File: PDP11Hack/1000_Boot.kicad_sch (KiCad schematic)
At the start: 19 parts, among them SW6 Boot Vector, U26 74HCT138, U27 74LS240

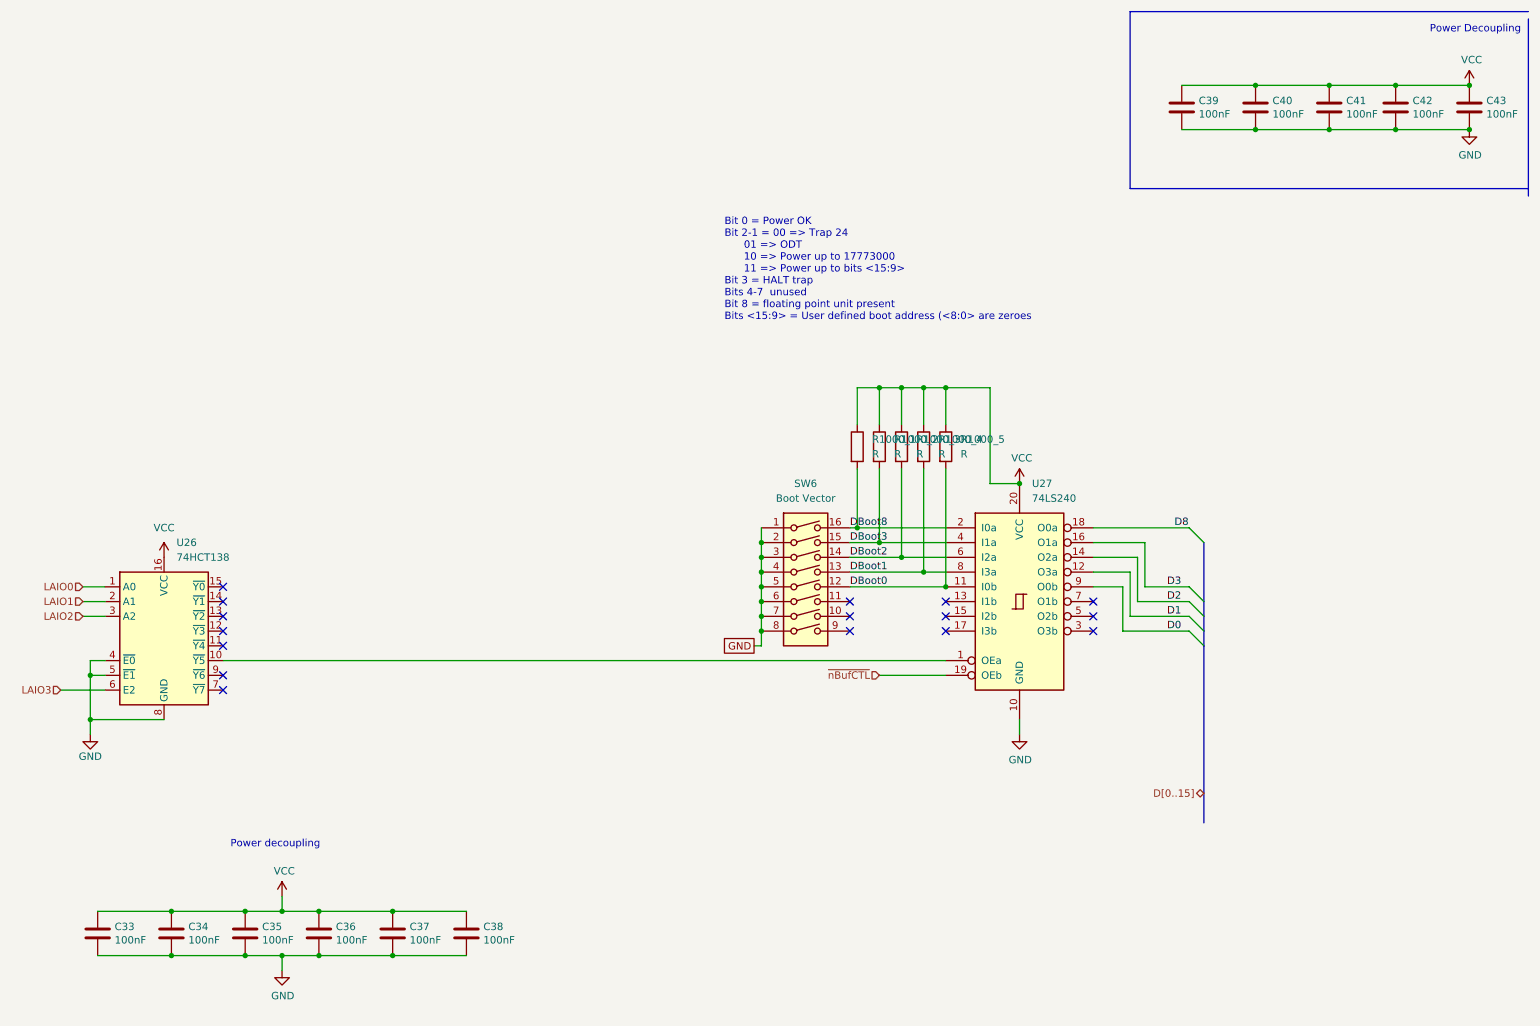
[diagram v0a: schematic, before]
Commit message: Corrections thanks to Peter Schranz on VCFED
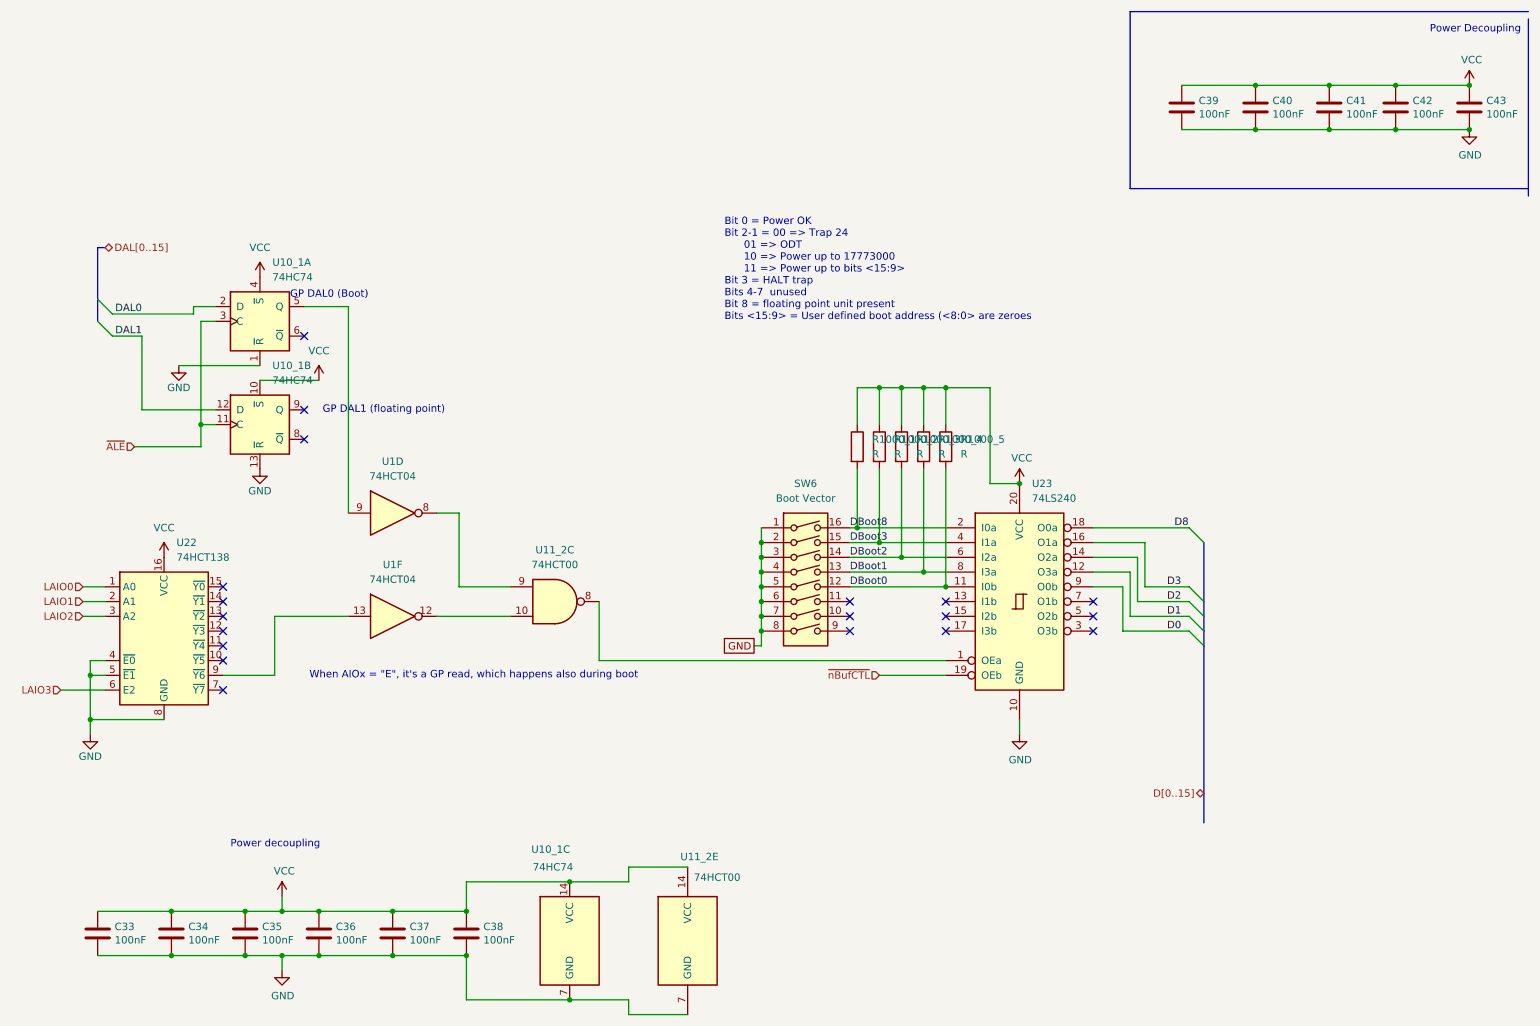
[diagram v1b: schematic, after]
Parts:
- added U1: 74HCT04, symbol 74xx:74HCT04
- added U10_1: 74HC74, symbol 74xx:74HC74
- added U11_2: 74HCT00, symbol 74xx:7400
- renumbered U26 to U22, U27 to U23
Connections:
- net GND: now also U10_1.1 (~{R}), U10_1.13 (~{R}), U10_1.7 (GND), U11_2.7 (GND)
- net VCC: now also U10_1.10 (~{S}), U10_1.14 (VCC), U10_1.4 (~{S}), U11_2.14 (VCC)
- net at U23.1 (OEa): now also U11_2.8; no longer U22.10 (~{Y5})
- net at U22.9 (~{Y6}): now also U1.13
- new net: U1.12, U11_2.10
- new net: U1.8, U11_2.9
- new net: U1.9, U10_1.5 (Q)
- new net DAL0: U10_1.2 (D)
- new net DAL1: U10_1.12 (D)
- new net ~{ALE}: U10_1.11 (C), U10_1.3 (C)
- no-connect marks 16 -> 19
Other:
- note added: "GP DAL0 (Boot)"
- note added: "GP DAL1 (floating point)"
- note added: "When AIOx = "E", it's a GP read, which happens also during boot"

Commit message: Last update, PCB creation ready
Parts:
- R1000_1, R1000_2, R1000_3, R1000_4, R1000_5: footprint (none) -> Resistor_THT:R_Axial_DIN0204_L3.6mm_D1.6mm_P7.62mm_Horizontal
- U1, U10_1, U11_2: footprint (none) -> Package_DIP:DIP-14_W7.62mm
- U22: footprint (none) -> Package_DIP:DIP-16_W7.62mm
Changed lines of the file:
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@@
 			)
 		)
-		(property "Footprint" ""
+		(property "Footprint" "Package_DIP:DIP-14_W7.62mm"
 			(at 60.96 86.36 0)
 			(effects
@@
 			)
 		)
-		(property "Footprint" ""
+		(property "Footprint" "Package_DIP:DIP-14_W7.62mm"
 			(at 111.76 116.84 0)
 			(effects
@@
 			)
 		)
-		(property "Footprint" ""
+		(property "Footprint" "Package_DIP:DIP-16_W7.62mm"
 			(at 44.45 124.46 0)
 			(effects
@@
 		(on_board yes)
 		(dnp no)
-		(fields_autoplaced yes)
 		(property "Reference" "R1000_5"
-			(at 181.61 88.9 0)
+			(at 179.07 85.09 0)
 			(effects
 				(font
@@
 			)
 		)
-		(property "Footprint" ""
+		(property "Footprint" "Resistor_THT:R_Axial_DIN0204_L3.6mm_D1.6mm_P7.62mm_Horizontal"
 			(at 177.292 90.17 90)
 			(effects
@@
 			)
 		)
-		(property "Footprint" ""
+		(property "Footprint" "Package_DIP:DIP-14_W7.62mm"
 			(at 134.62 175.26 0)
 			(effects
@@
 		(on_board yes)
 		(dnp no)
-		(fields_autoplaced yes)
 		(property "Reference" "R1000_1"
-			(at 166.37 88.9 0)
+			(at 163.83 84.074 0)
 			(effects
 				(font
@@
 			)
 		)
-		(property "Footprint" ""
+		(property "Footprint" "Resistor_THT:R_Axial_DIN0204_L3.6mm_D1.6mm_P7.62mm_Horizontal"
 			(at 162.052 90.17 90)
 			(effects
@@
 			)
 		)
-		(property "Footprint" ""
+		(property "Footprint" "Package_DIP:DIP-14_W7.62mm"
 			(at 83.82 119.38 0)
 			(effects
@@
 			)
 		)
-		(property "Footprint" ""
+		(property "Footprint" "Package_DIP:DIP-14_W7.62mm"
 			(at 60.96 68.58 0)
 			(effects
@@
 		(on_board yes)
 		(dnp no)
-		(fields_autoplaced yes)
 		(property "Reference" "R1000_2"
-			(at 170.18 88.9 0)
+			(at 167.894 81.788 0)
 			(effects
 				(font
@@
 			)
 		)
-		(property "Footprint" ""
+		(property "Footprint" "Resistor_THT:R_Axial_DIN0204_L3.6mm_D1.6mm_P7.62mm_Horizontal"
 			(at 165.862 90.17 90)
 			(effects
@@
 		(on_board yes)
 		(dnp no)
-		(fields_autoplaced yes)
 		(property "Reference" "R1000_3"
-			(at 173.99 88.9 0)
+			(at 171.45 86.36 0)
 			(effects
 				(font
@@
 			)
 		)
-		(property "Footprint" ""
+		(property "Footprint" "Resistor_THT:R_Axial_DIN0204_L3.6mm_D1.6mm_P7.62mm_Horizontal"
 			(at 169.672 90.17 90)
 			(effects
@@
 			)
 		)
-		(property "Footprint" ""
+		(property "Footprint" "Package_DIP:DIP-14_W7.62mm"
 			(at 83.82 101.6 0)
 			(effects
@@
 			)
 		)
-		(property "Footprint" ""
+		(property "Footprint" "Package_DIP:DIP-14_W7.62mm"
 			(at 114.3 175.26 0)
 			(effects
@@
 		(on_board yes)
 		(dnp no)
-		(fields_autoplaced yes)
 		(property "Reference" "R1000_4"
-			(at 177.8 88.9 0)
+			(at 175.768 83.312 0)
 			(effects
 				(font
@@
 			)
 		)
-		(property "Footprint" ""
+		(property "Footprint" "Resistor_THT:R_Axial_DIN0204_L3.6mm_D1.6mm_P7.62mm_Horizontal"
 			(at 173.482 90.17 90)
 			(effects
